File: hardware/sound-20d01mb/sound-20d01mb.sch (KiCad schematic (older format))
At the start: 14 parts

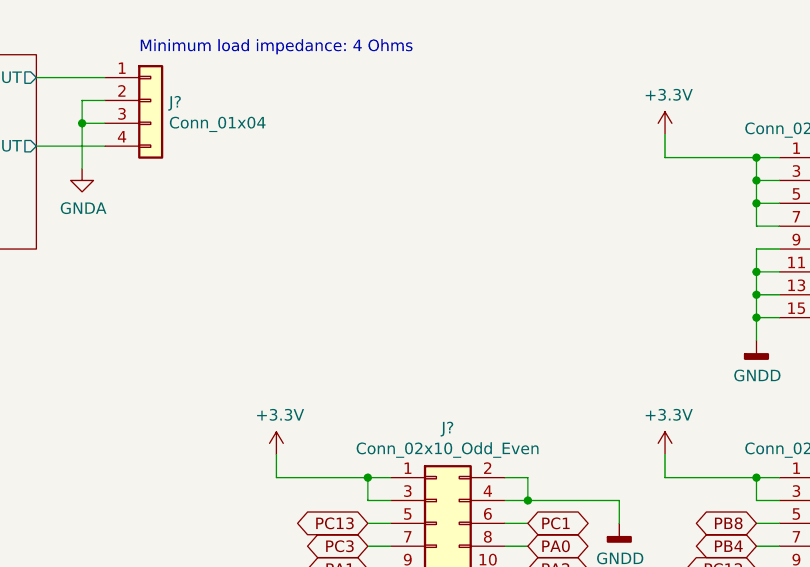
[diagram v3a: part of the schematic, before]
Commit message: Added connector for +5VA
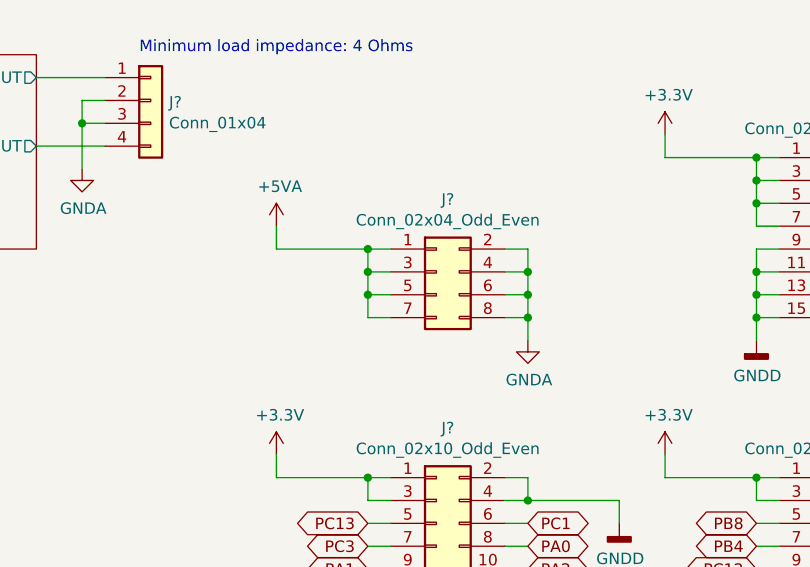
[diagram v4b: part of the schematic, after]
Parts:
- added J?: Conn_02x04_Odd_Even, Connector_PinHeader_2.54mm:PinHeader_2x04_P2.54mm_Vertical, symbol Connector_Generic:Conn_02x04_Odd_Even
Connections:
- net GNDA: now also J?.2 (Pin_2), J?.4 (Pin_4), J?.6 (Pin_6), J?.8 (Pin_8)
- new net +5VA: J?.1 (Pin_1), J?.3 (Pin_3), J?.5 (Pin_5), J?.7 (Pin_7)
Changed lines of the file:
@@
 Text GLabel 7300 5250 1    50   Output ~ 0
 RTC_VBAT
+$Comp
+L Connector_Generic:Conn_02x04_Odd_Even J?
+U 1 1 61A1BC0A
+P 8000 2650
+F 0 "J?" H 8050 2967 50  0000 C CNN
+F 1 "Conn_02x04_Odd_Even" H 8050 2876 50  0000 C CNN
+F 2 "Connector_PinHeader_2.54mm:PinHeader_2x04_P2.54mm_Vertical" H 8000 2650 50  0001 C CNN
+F 3 "~" H 8000 2650 50  0001 C CNN
+	1    8000 2650
+	1    0    0    -1
+$EndComp
+$Comp
+L power:+5VA #PWR?
+U 1 1 61A21C9A
+P 7300 2450
+AR Path="/60DE2DF4/61A21C9A" Ref="#PWR?"  Part="1"
+AR Path="/61033008/61A21C9A" Ref="#PWR?"  Part="1"
+F 0 "#PWR?" H 7300 2300 50  0001 C CNN
+F 1 "+5VA" H 7315 2623 50  0000 C CNN
+F 2 "" H 7300 2450 50  0001 C CNN
+F 3 "" H 7300 2450 50  0001 C CNN
+	1    7300 2450
+	1    0    0    -1
+$EndComp
+Wire Wire Line
+	7300 2550 7300 2450
+Wire Wire Line
+	7300 2550 7700 2550
+Wire Wire Line
+	7800 2650 7700 2650
+Wire Wire Line
+	7700 2650 7700 2550
+Connection ~ 7700 2550
+Wire Wire Line
+	7700 2550 7800 2550
+Wire Wire Line
+	7800 2750 7700 2750
+Wire Wire Line
+	7700 2750 7700 2650
+Connection ~ 7700 2650
+Wire Wire Line
+	7800 2850 7700 2850
+Wire Wire Line
+	7700 2850 7700 2750
+Connection ~ 7700 2750
+$Comp
+L power:GNDA #PWR?
+U 1 1 61A4ACD4
+P 8400 2950
+F 0 "#PWR?" H 8400 2700 50  0001 C CNN
+F 1 "GNDA" H 8405 2777 50  0000 C CNN
+F 2 "" H 8400 2950 50  0001 C CNN
+F 3 "" H 8400 2950 50  0001 C CNN
+	1    8400 2950
+	1    0    0    -1
+$EndComp
+Wire Wire Line
+	8300 2850 8400 2850
+Wire Wire Line
+	8400 2850 8400 2950
+Wire Wire Line
+	8300 2750 8400 2750
+Wire Wire Line
+	8400 2750 8400 2850
+Connection ~ 8400 2850
+Wire Wire Line
+	8300 2650 8400 2650
+Wire Wire Line
+	8400 2650 8400 2750
+Connection ~ 8400 2750
+Wire Wire Line
+	8300 2550 8400 2550
+Wire Wire Line
+	8400 2550 8400 2650
+Connection ~ 8400 2650
 $EndSCHEMATC

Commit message: Annotate schematic
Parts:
- gave numbers to parts that had none: 15
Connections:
- net RTC_VBAT renamed +BATT
